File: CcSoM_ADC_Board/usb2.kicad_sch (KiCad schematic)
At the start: 12 parts, among them J18 USB_A, J19 USB_A, U10 USB3343

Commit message: corrected schematic created pdf and bom file
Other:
- company: (none) -> Technische Hochschule Köln
- title: (none) -> SoM Programmer & ADC Board
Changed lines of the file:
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@@
 	(generator_version "9.0")
 	(paper "A4")
+	(title_block
+		(title "SoM Programmer & ADC Board")
+		(date "2026-02-09")
+		(rev "0.1")
+		(company "Technische Hochschule Köln")
+		(comment 1 "Ismail Özdemirkan")
+	)
 	(junction
 		(at 36.83 72.39)

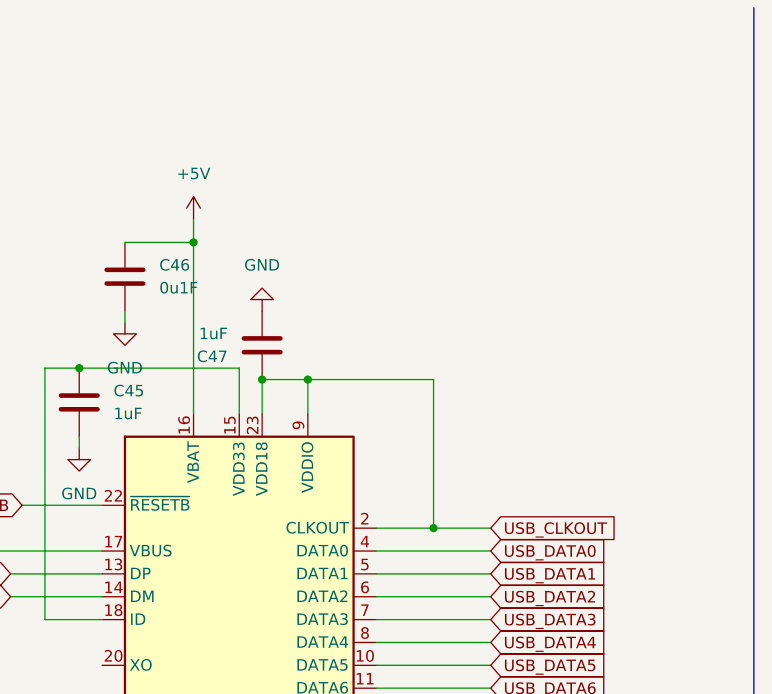
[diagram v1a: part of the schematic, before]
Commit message: moved designator and changed vddio to 2.5V
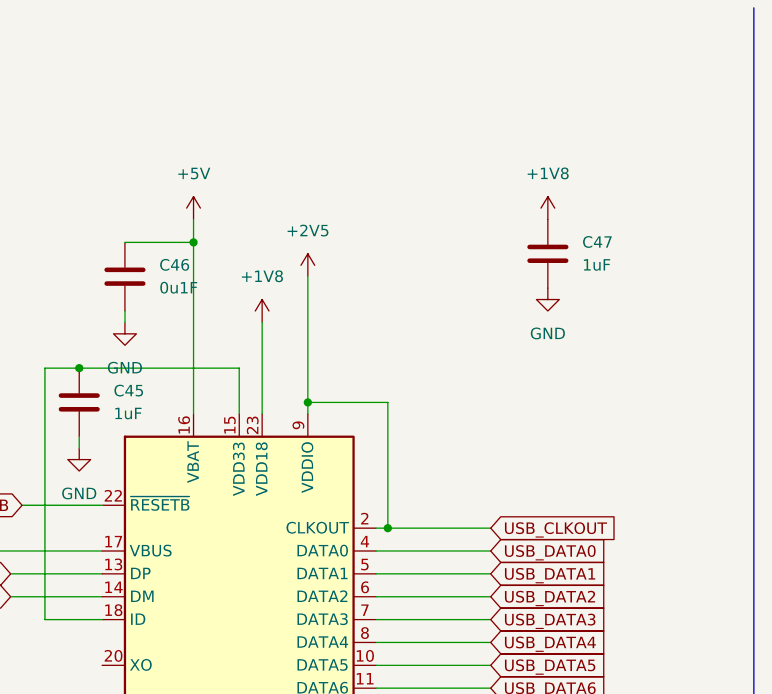
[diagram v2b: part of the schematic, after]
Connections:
- net USB_CLKOUT renamed +1V8
- net +1V8: no longer U10.2 (CLKOUT), U10.9 (VDDIO)
- new net +2V5: U10.2 (CLKOUT), U10.9 (VDDIO)
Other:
- moved on the sheet: C47

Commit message: last before rotating adc
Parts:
- added U9: TXS0202YZPR, YZP8, symbol TXS0202YZPR:TXS0202YZPR
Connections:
- net +2V5: now also U9.C1 (VCCA), U9.C2 (OE)
- net GND: now also U9.B1 (GND)
- net USB2_+: now also U9.D2 (D-(A)); no longer J18.3 (D+)
- net USB2_-: now also U9.D1 (D+(A)); no longer J18.2 (D-)
- new net +3V3: U9.B2 (VCCB)
- new net D_+: J18.2 (D-), U9.A2 (D-(B))
- new net D_-: J18.3 (D+), U9.A1 (D+(B))
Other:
- note added: "D+ and D- is inverted"

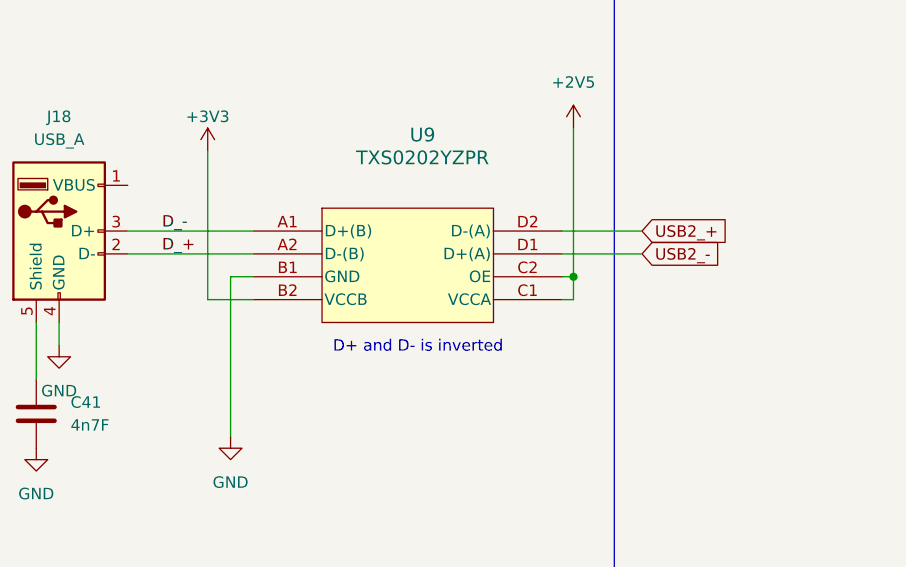
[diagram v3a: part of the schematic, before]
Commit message: changed schottky, began to add digikey part numbers
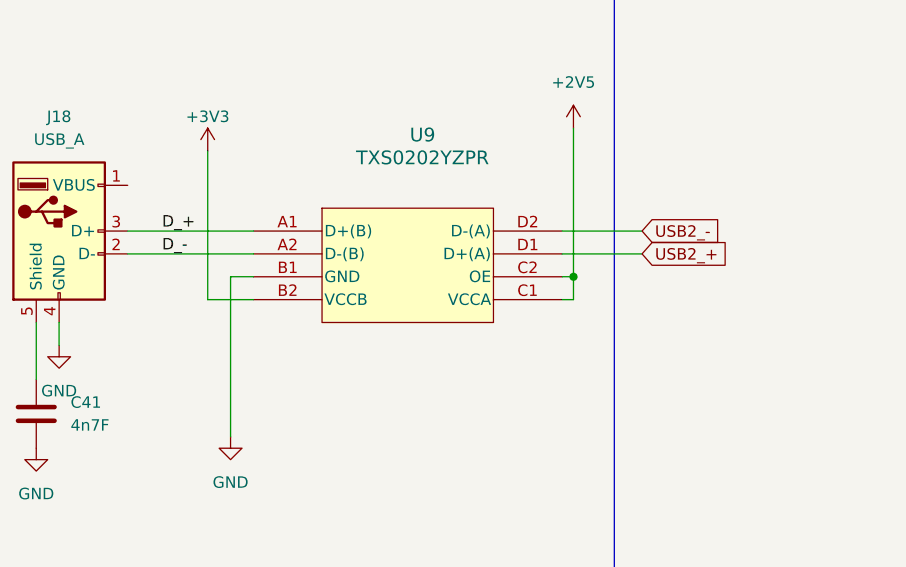
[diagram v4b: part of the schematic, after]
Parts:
- D15: footprint Diode_SMD:D_0603_1608Metric_Pad1.05x0.95mm_HandSolder -> Diode_SMD:D_0805_2012Metric_Pad1.15x1.40mm_HandSolder; DigiKey_no (none) -> 478-7800-1-ND
- J18, J19: DigiKey_no (none) -> 380-1412-ND
- R30: DigiKey_no (none) -> RMCF0603FT1K00CT-ND
- U10: DigiKey_no (none) -> 638-1116-1-ND
- U9: DigiKey_no (none) -> 296-29072-1-ND
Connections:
- net D_+: now also J18.3 (D+), U9.A1 (D+(B)); no longer J18.2 (D-), U9.A2 (D-(B))
- net D_-: now also J18.2 (D-), U9.A2 (D-(B)); no longer J18.3 (D+), U9.A1 (D+(B))
- net USB2_+: now also U9.D1 (D+(A)); no longer U9.D2 (D-(A))
- net USB2_-: now also U9.D2 (D-(A)); no longer U9.D1 (D+(A))
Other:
- note removed: "D+ and D- is inverted"
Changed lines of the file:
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@@
 		(comment 1 "Ismail Özdemirkan")
 	)
-	(text "D+ and D- is inverted"
-		(exclude_from_sim no)
-		(at 75.438 166.624 0)
-		(effects
-			(font
-				(size 1.27 1.27)
-			)
-		)
-	)
 	(junction
 		(at 92.71 158.75)
@@
 		)
 	)
-	(label "D_+"
+	(label "D_-"
 		(at 46.99 156.21 0)
 		(effects
@@
 		)
 	)
-	(label "D_-"
+	(label "D_+"
 		(at 46.99 153.67 0)
 		(effects
@@
 		)
 	)
-	(global_label "USB_DATA0"
+	(global_label "USB2_-"
 		(shape input)
-		(at 114.3 72.39 0)
+		(at 100.33 153.67 0)
 		(fields_autoplaced yes)
 		(effects
@@
 		)
 		(property "Intersheetrefs" "${INTERSHEET_REFS}"
-			(at 127.6871 72.39 0)
+			(at 110.8747 153.67 0)
 			(effects
 				(font
@@
 		)
 	)
-	(global_label "USB2_-"
+	(global_label "USB_DATA0"
 		(shape input)
-		(at 100.33 156.21 0)
+		(at 114.3 72.39 0)
 		(fields_autoplaced yes)
 		(effects
@@
 		)
 		(property "Intersheetrefs" "${INTERSHEET_REFS}"
-			(at 110.8747 156.21 0)
+			(at 127.6871 72.39 0)
 			(effects
 				(font
@@
 		)
 	)
-	(global_label "USB2_+"
+	(global_label "USB_DATA2"
 		(shape input)
-		(at 100.33 153.67 0)
+		(at 114.3 77.47 0)
 		(fields_autoplaced yes)
 		(effects
@@
 		)
 		(property "Intersheetrefs" "${INTERSHEET_REFS}"
-			(at 110.8747 153.67 0)
+			(at 127.6871 77.47 0)
 			(effects
 				(font
@@
 		)
 	)
-	(global_label "USB_DATA2"
+	(global_label "USB2_+"
 		(shape input)
-		(at 114.3 77.47 0)
+		(at 100.33 156.21 0)
 		(fields_autoplaced yes)
 		(effects
@@
 		)
 		(property "Intersheetrefs" "${INTERSHEET_REFS}"
-			(at 127.6871 77.47 0)
+			(at 110.8747 156.21 0)
 			(effects
 				(font
@@
 			)
 		)
-		(property "Footprint" "Diode_SMD:D_0603_1608Metric_Pad1.05x0.95mm_HandSolder"
+		(property "Footprint" "Diode_SMD:D_0805_2012Metric_Pad1.15x1.40mm_HandSolder"
 			(at 43.18 72.39 0)
 			(effects
@@
 			)
 		)
-		(property "Datasheet" "~"
+		(property "Datasheet" "https://datasheets.kyocera-avx.com/schottky.pdf"
 			(at 43.18 72.39 0)
 			(effects
@@
 			)
 		)
+		(property "DigiKey_no" "478-7800-1-ND"
+			(at 43.18 72.39 0)
+			(effects
+				(font
+					(size 1.27 1.27)
+				)
+				(hide yes)
+			)
+		)
 		(pin "1"
 		)
@@
 			)
 		)
+		(property "DigiKey_no" "380-1412-ND"
+			(at 25.4 77.47 0)
+			(effects
+				(font
+					(size 1.27 1.27)
+				)
+				(hide yes)
+			)
+		)
 		(pin "2"
 		)
@@
 			)
 		)
+		(property "DigiKey_no" "RMCF0603FT1K00CT-ND"
+			(at 54.61 72.39 90)
+			(effects
+				(font
+					(size 1.27 1.27)
+				)
+				(hide yes)
+			)
+		)
 		(pin "2"
 		)
@@
 			)
 		)
+		(property "DigiKey_no" "638-1116-1-ND "
+			(at 86.36 80.01 0)
+			(effects
+				(font
+					(size 1.27 1.27)
+				)
+				(hide yes)
+			)
+		)
 		(pin "20"
 		)
@@
 			)
 		)
+		(property "DigiKey_no" "296-29072-1-ND"
+			(at 57.15 153.67 0)
+			(effects
+				(font
+					(size 1.27 1.27)
+				)
+				(hide yes)
+			)
+		)
 		(pin "C2"
 		)
@@
 			(at 35.56 153.67 0)
 			(effects
+				(font
+					(size 1.27 1.27)
+				)
+				(hide yes)
+			)
+		)
+		(property "DigiKey_no" "380-1412-ND"
+			(at 35.56 153.67 0)
+			(effects

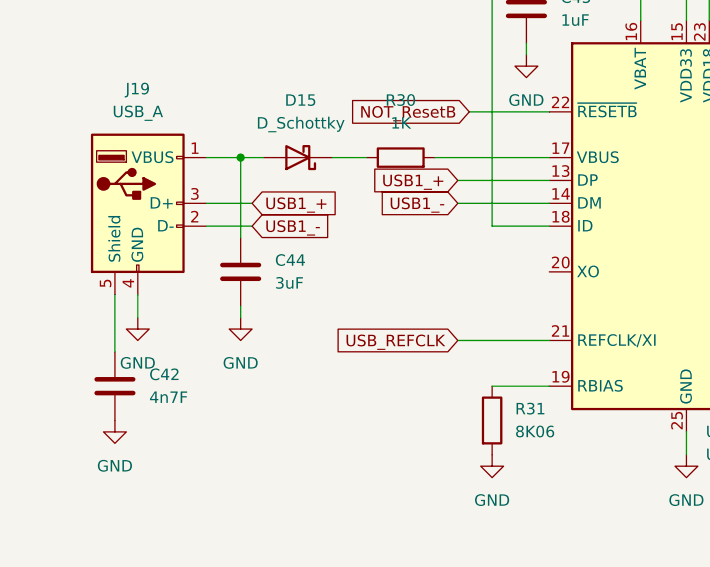
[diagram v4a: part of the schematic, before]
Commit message: digikey no not complete
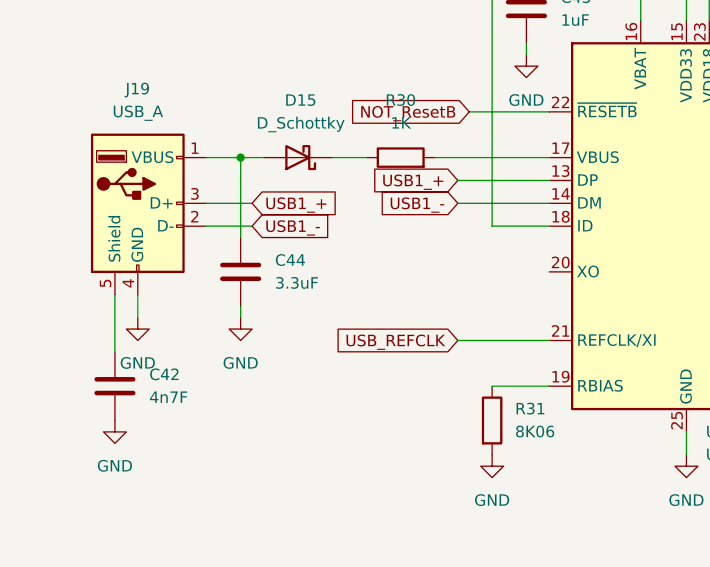
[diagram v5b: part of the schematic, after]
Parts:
- C41, C42: DigiKey_no (none) -> 399-C0603C472K5RACTUCT-ND
- C44: value 3uF -> 3.3uF; DigiKey_no (none) -> 399-3481-1-ND
- C45, C47: DigiKey_no (none) -> 399-C0603C105K4RACTUCT-ND
- C46: DigiKey_no (none) -> 311-1088-1-ND
- R31: DigiKey_no (none) -> 541-8.06KHCT-ND
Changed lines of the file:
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@@
+			)
+		)
+		(property "DigiKey_no" "399-C0603C472K5RACTUCT-ND"
+			(at 22.86 97.79 0)
+			(effects
+				(font
+					(size 1.27 1.27)
+				)
+				(hide yes)
 			)
 		)
@@
 			)
 		)
+		(property "DigiKey_no" "399-C0603C105K4RACTUCT-ND"
+			(at 68.58 55.88 0)
+			(effects
+				(font
+					(size 1.27 1.27)
+				)
+				(hide yes)
+			)
+		)
 		(pin "1"
 		)
@@
 			)
 		)
+		(property "DigiKey_no" "399-C0603C105K4RACTUCT-ND"
+			(at 120.65 39.37 0)
+			(effects
+				(font
+					(size 1.27 1.27)
+				)
+				(hide yes)
+			)
+		)
 		(pin "1"
 		)
@@
 			)
 		)
+		(property "DigiKey_no" "541-8.06KHCT-ND"
+			(at 64.77 101.6 0)
+			(effects
+				(font
+					(size 1.27 1.27)
+				)
+				(hide yes)
+			)
+		)
 		(pin "1"
 		)
@@
 			)
 		)
-		(property "Value" "3uF"
+		(property "Value" "3.3uF"
 			(at 40.64 86.3599 0)
 			(effects
@@
 			)
 		)
+		(property "DigiKey_no" "399-3481-1-ND"
+			(at 36.83 85.09 0)
+			(effects
+				(font
+					(size 1.27 1.27)
+				)
+				(hide yes)
+			)
+		)
 		(pin "1"
 		)
@@
 			)
 		)
+		(property "DigiKey_no" "311-1088-1-ND"
+			(at 73.66 41.91 0)
+			(effects
+				(font
+					(size 1.27 1.27)
+				)
+				(hide yes)
+			)
+		)
 		(pin "1"
 		)
@@
 			(at 33.02 173.99 0)
 			(effects
+				(font
+					(size 1.27 1.27)
+				)
+				(hide yes)
+			)
+		)
+		(property "DigiKey_no" "399-C0603C472K5RACTUCT-ND"
+			(at 33.02 173.99 0)
+			(effects

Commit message: changed digikeyno from component, added info into readme about discontinued parts in digikey
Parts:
- U9: Mouser Part Number (none) -> 595-TXS0202YZPR
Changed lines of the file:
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@@
+			)
+		)
+		(property "Mouser Part Number" "595-TXS0202YZPR"
+			(at 57.15 153.67 0)
+			(effects
+				(font
+					(size 1.27 1.27)
+				)
+				(hide yes)
 			)
 		)
